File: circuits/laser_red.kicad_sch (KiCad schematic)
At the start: 10 parts, among them Q2 AO3400A, U6 TLV9001

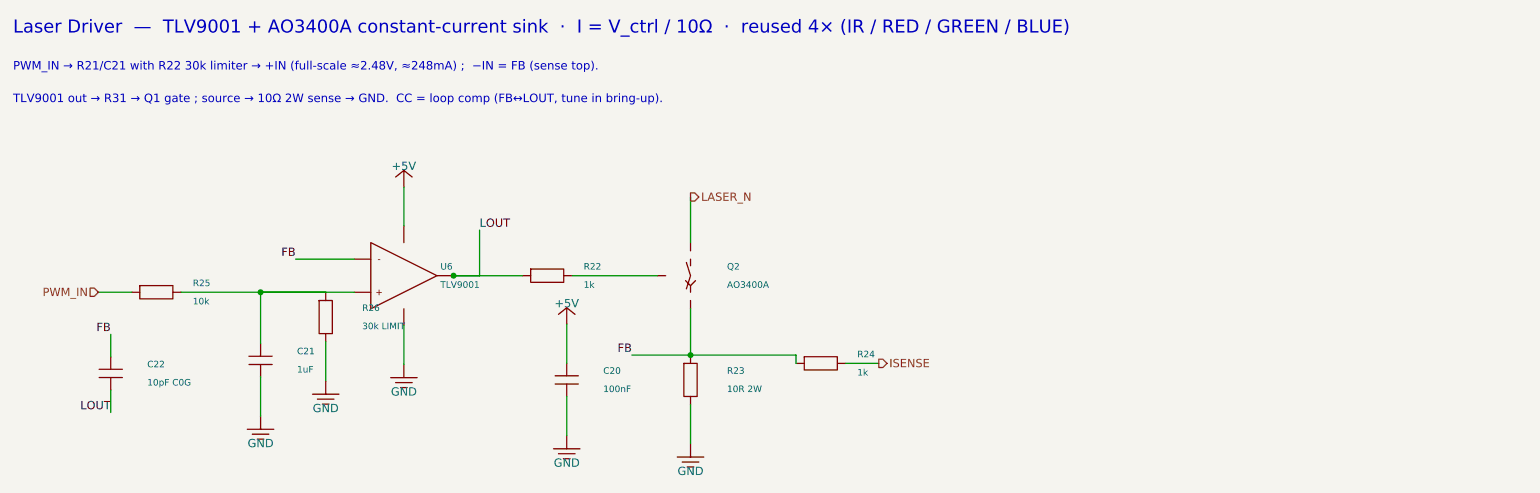
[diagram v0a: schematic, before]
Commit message: chore(circuits): update laser controller release artifacts
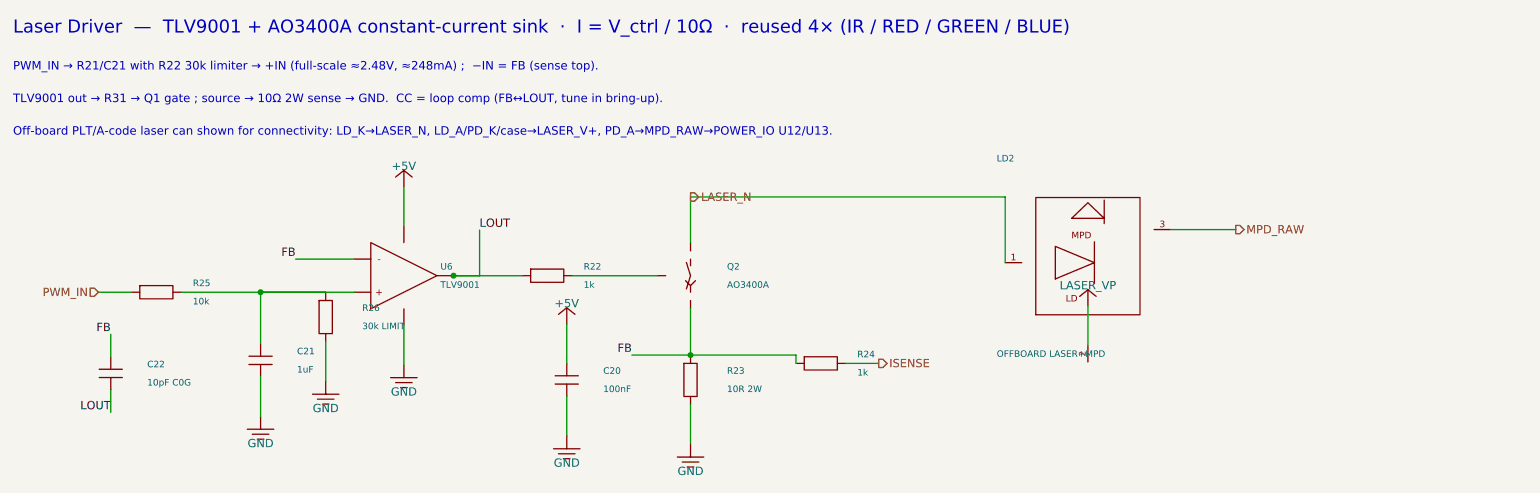
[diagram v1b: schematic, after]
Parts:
- removed C20: 100nF, Capacitor_SMD:C_0402_1005Metric_Pad0.74x0.62mm_HandSolder, symbol viv:C_V
- removed R26: 30k LIMIT, Resistor_SMD:R_0603_1608Metric_Pad0.98x0.95mm_HandSolder, symbol viv:R_V
- removed U6: TLV9001, Package_TO_SOT_SMD:SOT-23-5, symbol viv:TLV9001_SOT23_5
- added C22: 10pF C0G, Capacitor_SMD:C_0603_1608Metric_Pad1.08x0.95mm_HandSolder, symbol viv:C_V
- added R22, R24: 1k, Resistor_SMD:R_0603_1608Metric_Pad0.98x0.95mm_HandSolder, symbol viv:R_H
- added R23: 10R 2W, Resistor_SMD:R_2512_6332Metric_Pad1.40x3.35mm_HandSolder, symbol viv:R_V
- C20: renamed from C22; value 10pF C0G -> 100nF; footprint Capacitor_SMD:C_0603_1608Metric_Pad1.08x0.95mm_HandSolder -> Capacitor_SMD:C_0402_1005Metric_Pad0.74x0.62mm_HandSolder; LCSC C106245 -> C1525; Part Number CC0603JRNPO9BN100 -> CL05B104KO5NNNC
- C21: renamed from R24; value 1k -> 1uF; footprint Resistor_SMD:R_0603_1608Metric_Pad0.98x0.95mm_HandSolder -> Capacitor_SMD:C_0402_1005Metric_Pad0.74x0.62mm_HandSolder; symbol viv:R_H -> viv:C_V; LCSC C21190 -> C52923; Part Number 0603WAF1001T5E -> CL05A105KA5NQNC
- LD2: renamed from R22; value 1k -> OFFBOARD LASER+MPD; footprint Resistor_SMD:R_0603_1608Metric_Pad0.98x0.95mm_HandSolder -> (none); symbol viv:R_H -> viv:LASER_CAN_MON_PD; LCSC C21190 -> (none); Part Number 0603WAF1001T5E -> (none); now left out of the parts list
- R26: renamed from R23; value 10R 2W -> 30k LIMIT; footprint Resistor_SMD:R_2512_6332Metric_Pad1.40x3.35mm_HandSolder -> Resistor_SMD:R_0603_1608Metric_Pad0.98x0.95mm_HandSolder; LCSC C5123624 -> C22984; Part Number HoCR2512-2W-10R-1% -> 0603WAF3002T5E
- U6: renamed from C21; value 1uF -> TLV9001; footprint Capacitor_SMD:C_0402_1005Metric_Pad0.74x0.62mm_HandSolder -> Package_TO_SOT_SMD:SOT-23-5; symbol viv:C_V -> viv:TLV9001_SOT23_5; LCSC C52923 -> C398363; Part Number CL05A105KA5NQNC -> TLV9001IDBVR
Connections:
- net +5V: now also C20.1, U6.5 (V+)
- net FB: now also U6.4 (-), C22.1, R23.1, R24.1; no longer C20.1, C21.1, R26.1
- net GND: now also C20.2, C21.2, R23.2
- net ISENSE: now also R24.2; no longer C21.2
- net LASER_N: now also LD2.1 (LD_K)
- net LOUT: now also U6.1, C22.2, R22.1; no longer C20.2, LD2.1
- net at R25.2: now also C21.1, R26.1, U6.3 (+); no longer U6.1
- net at Q2.1 (G): now also R22.2; no longer LD2.2
- new net LASER_V+: LD2.2 (LD_A/PD_K/CASE)
- new net MPD_RAW: LD2.3 (PD_A)
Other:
- note added: "Off-board PLT/A-code laser can shown for connectivity: LD_K→LASER_N, LD_A/PD_K/case→LASER_V+, PD_A→MPD_RAW→POWER_IO U12/U13."
- moved on the sheet: C20, R26
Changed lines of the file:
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@@
+    )
+  )
+  (symbol (lib_id "viv:LASER_CAN_MON_PD") (at 315 150 0) (unit 1)
+    (in_bom no) (on_board yes) (dnp no)
+    (property "Reference" "LD2" (at 301 134 0) (effects (font (size 1.0 1.0)) (justify left)))
+    (property "Value" "OFFBOARD LASER+MPD" (at 301 164 0) (effects (font (size 1.0 1.0)) (justify left)))
+    (property "Footprint" "" (at 315 150 0) (effects (font (size 1.0 1.0)) hide))
+    (property "Datasheet" "" (at 315 150 0) (effects (font (size 1.0 1.0)) hide))
+    (property "Part Number" "" (at 315 150 0) (effects (font (size 1.0 1.0)) hide))
+    (property "LCSC" "" (at 315 150 0) (effects (font (size 1.0 1.0)) hide))
+    (pin "1")
+    (pin "2")
+    (pin "3")
+    (instances
+      (project "laser_controller"
+        (path "/c1d2e3f4-6000-4000-a000-000000000001" (reference "LD2") (unit 1))
+      )
     )
   )
@@
       (project "laser_controller"
         (path "/c1d2e3f4-6000-4000-a000-000000000001" (reference "#PWR07") (unit 1))
+      )
+    )
+  )
+  (symbol (lib_id "viv:LASER_VP") (at 315 156.7 0) (unit 1)
+    (in_bom no) (on_board yes) (dnp no)
+    (property "Reference" "#PWR08" (at 315 153.7 0) (effects (font (size 1.0 1.0)) hide))
+    (property "Value" "LASER_VP" (at 315 153.5 0) (effects (font (size 1.27 1.27))))
+    (property "Footprint" "" (at 0 0 0) (effects (font (size 1.0 1.0)) hide))
+    (property "Datasheet" "" (at 0 0 0) (effects (font (size 1.0 1.0)) hide))
+    (pin "1")
+    (instances
+      (project "laser_controller"
+        (path "/c1d2e3f4-6000-4000-a000-000000000001" (reference "#PWR08") (unit 1))
       )
     )
@@
   (wire (pts (xy 277.81 165.46) (xy 282.89 165.46)) (stroke (width 0) (type default)))
   (wire (pts (xy 254 146.92) (xy 254 139.92)) (stroke (width 0) (type default)))
+  (wire (pts (xy 254 139.92) (xy 302.3 139.92)) (stroke (width 0) (type default)))
+  (wire (pts (xy 302.3 139.92) (xy 302.3 150)) (stroke (width 0) (type default)))
+  (wire (pts (xy 315 162.7) (xy 315 156.7)) (stroke (width 0) (type default)))
+  (wire (pts (xy 327.7 144.92) (xy 337.7 144.92)) (stroke (width 0) (type default)))
   (wire (pts (xy 202.38 149.46) (xy 193.38 149.46)) (stroke (width 0) (type default)))
   (wire (pts (xy 254 164.19) (xy 245 164.19)) (stroke (width 0) (type default)))
@@
   (hierarchical_label "ISENSE" (shape output) (at 282.89 165.46 0) (effects (font (size 1.27 1.27)) (justify left)))
   (hierarchical_label "LASER_N" (shape output) (at 254 139.92 0) (effects (font (size 1.27 1.27)) (justify left)))
+  (hierarchical_label "MPD_RAW" (shape output) (at 337.7 144.92 0) (effects (font (size 1.27 1.27)) (justify left)))
   (label "FB" (at 193.38 149.46 0) (effects (font (size 1.27 1.27)) (justify right bottom)))
   (label "FB" (at 245 164.19 0) (effects (font (size 1.27 1.27)) (justify right bottom)))
@@
   (text "PWM_IN → R21/C21 with R22 30k limiter → +IN (full-scale ≈2.48V, ≈248mA) ;  −IN = FB (sense top)." (at 150 120 0) (effects (font (size 1.3 1.3)) (justify left)))
   (text "TLV9001 out → R31 → Q1 gate ; source → 10Ω 2W sense → GND.  CC = loop comp (FB↔LOUT, tune in bring-up)." (at 150 125 0) (effects (font (size 1.3 1.3)) (justify left)))
+  (text "Off-board PLT/A-code laser can shown for connectivity: LD_K→LASER_N, LD_A/PD_K/case→LASER_V+, PD_A→MPD_RAW→POWER_IO U12/U13." (at 150 130 0) (effects (font (size 1.3 1.3)) (justify left)))
   (sheet_instances
     (path "/" (page "1"))

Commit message: fix(circuits): import mcu sheet and laser footprints
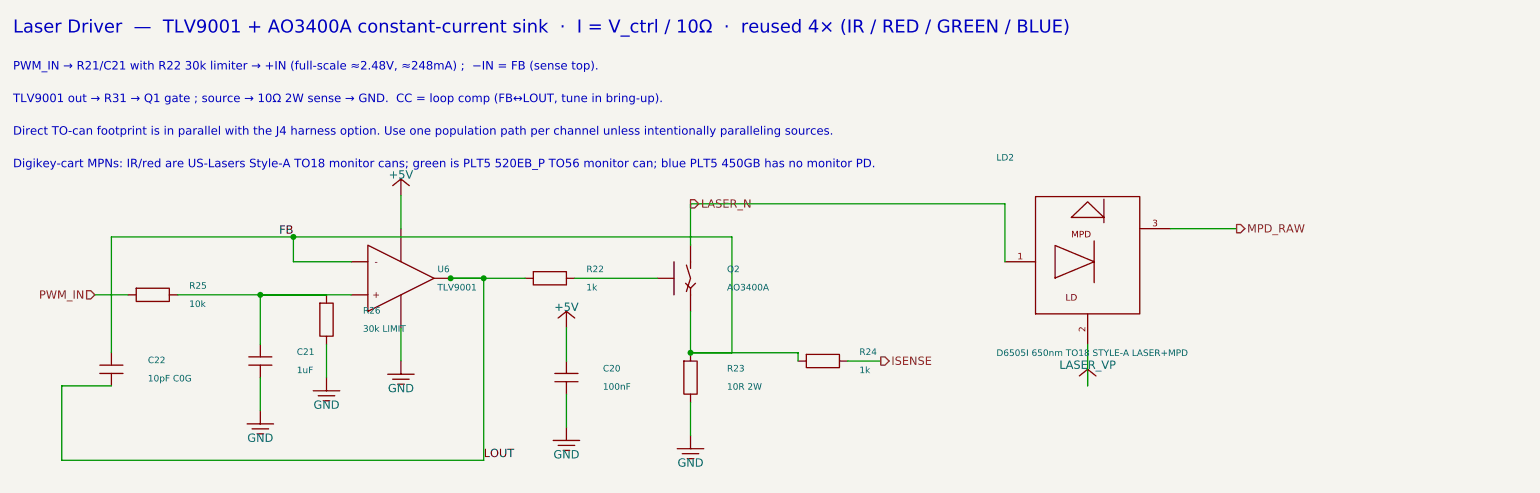
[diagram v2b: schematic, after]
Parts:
- C20: LCSC C1525 -> C83056; Part Number CL05B104KO5NNNC -> 0402B104K160CT
- C21: LCSC C52923 -> C7472946; Part Number CL05A105KA5NQNC -> HGC0402R5105K250NTEJ
- LD2: value OFFBOARD LASER+MPD -> D6505I 650nm TO18 STYLE-A LASER+MPD; footprint (none) -> OptoDevice:LaserDiode_TO18-D5.6-3; Part Number (none) -> D6505I
- R22, R24: LCSC C21190 -> C2907002; Part Number 0603WAF1001T5E -> FRC0603F1001TS
- R25: LCSC C269701 -> C844918; Part Number 0603WAF1002T5E -> CRCW060310K0FKEA
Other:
- note added: "Digikey-cart MPNs: IR/red are US-Lasers Style-A TO18 monitor cans; green is PLT5 520EB_P TO56 monitor can; blue PLT5 450GB has no monitor PD."
- note added: "Direct TO-can footprint is in parallel with the J4 harness option. Use one population path per channel unless intentionally paralleling sources."
- note removed: "Off-board PLT/A-code laser can shown for connectivity: LD_K→LASER_N, LD_A/PD_K/case→LASER_V+, PD_A→MPD_RAW→POWER_IO U12/U13."

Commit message: save laser controller schematic and layout state
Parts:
- removed R25: 10k, Resistor_SMD:R_0603_1608Metric_Pad0.98x0.95mm_HandSolder, symbol viv:R_H
- removed R26: 30k LIMIT, Resistor_SMD:R_0603_1608Metric_Pad0.98x0.95mm_HandSolder, symbol viv:R_V
- added Q2: AO3400A, Package_TO_SOT_SMD:SOT-23, symbol viv:NMOS
- added R22: 1k, Resistor_SMD:R_0603_1608Metric_Pad0.98x0.95mm_HandSolder, symbol viv:R_H
- R25: renamed from R22; value 1k -> 10k; LCSC C2907002 -> C844918; Part Number FRC0603F1001TS -> CRCW060310K0FKEA
- R26: renamed from Q2; value AO3400A -> 30k LIMIT; footprint Package_TO_SOT_SMD:SOT-23 -> Resistor_SMD:R_0603_1608Metric_Pad0.98x0.95mm_HandSolder; symbol viv:NMOS -> viv:R_V; LCSC C20917 -> C22984; Part Number AO3400A -> 0603WAF3002T5E
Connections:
- net FB: now also Q2.2 (S); no longer R26.2 (S)
- net GND: now also R26.2
- net LASER_N: now also Q2.3 (D); no longer R26.3 (D)
- net LOUT: now also R22.1; no longer R25.1
- net PWM_IN: now also R25.1
- net at C21.1, U6.3 (+): now also R25.2, R26.1
- new net: Q2.1 (G), R22.2
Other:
- moved on the sheet: R25

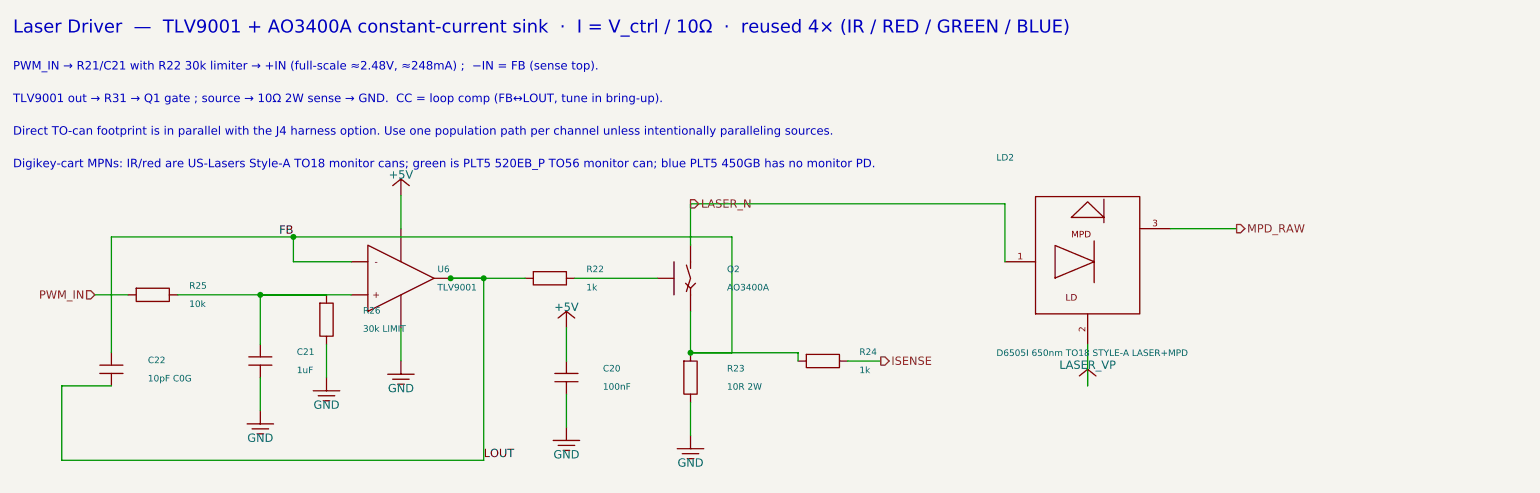
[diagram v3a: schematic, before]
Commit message: save current laser controller recovery state
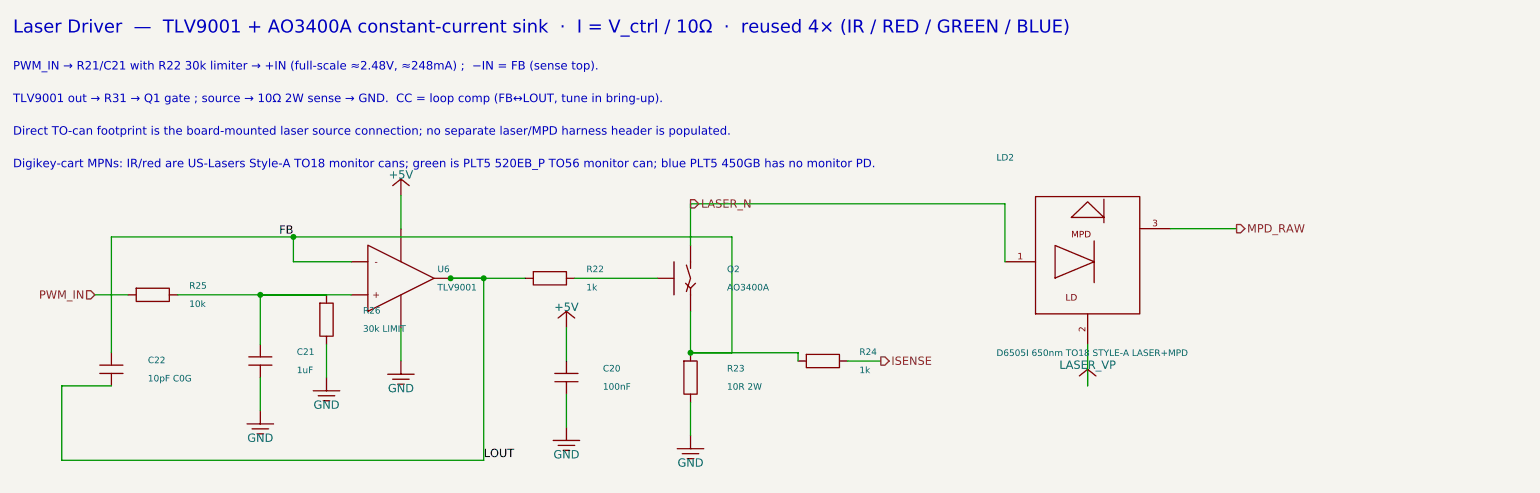
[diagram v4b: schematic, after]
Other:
- note added: "Direct TO-can footprint is the board-mounted laser source connection; no separate laser/MPD harness header is populated."
- note removed: "Direct TO-can footprint is in parallel with the J4 harness option. Use one population path per channel unless intentionally paralleling sources."
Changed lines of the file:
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@@
   (text "PWM_IN → R21/C21 with R22 30k limiter → +IN (full-scale ≈2.48V, ≈248mA) ;  −IN = FB (sense top)." (at 150 120 0) (effects (font (size 1.3 1.3)) (justify left)))
   (text "TLV9001 out → R31 → Q1 gate ; source → 10Ω 2W sense → GND.  CC = loop comp (FB↔LOUT, tune in bring-up)." (at 150 125 0) (effects (font (size 1.3 1.3)) (justify left)))
-  (text "Direct TO-can footprint is in parallel with the J4 harness option. Use one population path per channel unless intentionally paralleling sources." (at 150 130 0) (effects (font (size 1.3 1.3)) (justify left)))
+  (text "Direct TO-can footprint is the board-mounted laser source connection; no separate laser/MPD harness header is populated." (at 150 130 0) (effects (font (size 1.3 1.3)) (justify left)))
   (text "Digikey-cart MPNs: IR/red are US-Lasers Style-A TO18 monitor cans; green is PLT5 520EB_P TO56 monitor can; blue PLT5 450GB has no monitor PD." (at 150 135 0) (effects (font (size 1.3 1.3)) (justify left)))
   (sheet_instances
